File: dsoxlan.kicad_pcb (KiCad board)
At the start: 2 copper layers, 81.3 x 58.4 mm, 11 parts, among them P1 CNT-RJ45, P2 CONN_02X40

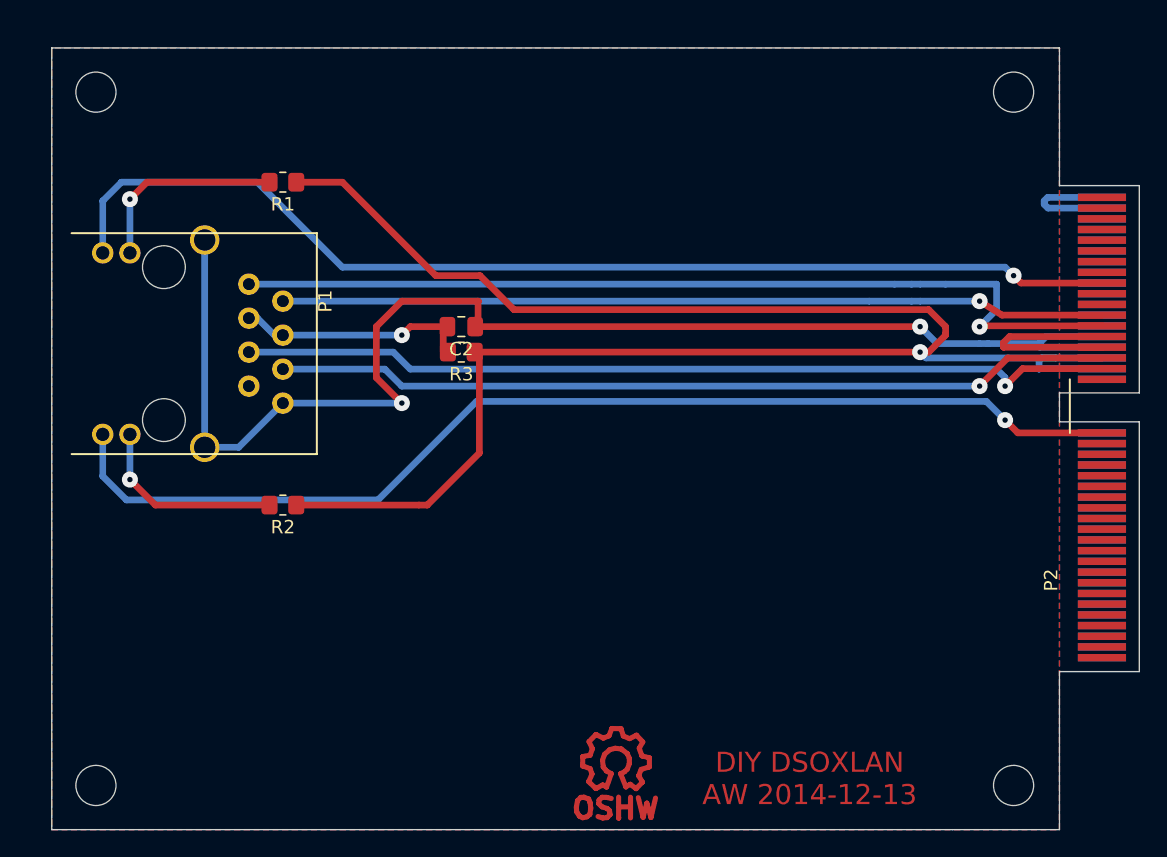
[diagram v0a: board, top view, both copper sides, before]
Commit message: DSC fixup
Replace all objects by new ones from the current libraries
shipped by Kicad.

This causes a slightly different OSHW (Opensource Hardware)
logo to be used in the PCB.

To maintain schematic parity, all mechanical objects on the
PCB (mounting holes and OSHW logo) have their schematic
counterparts now.
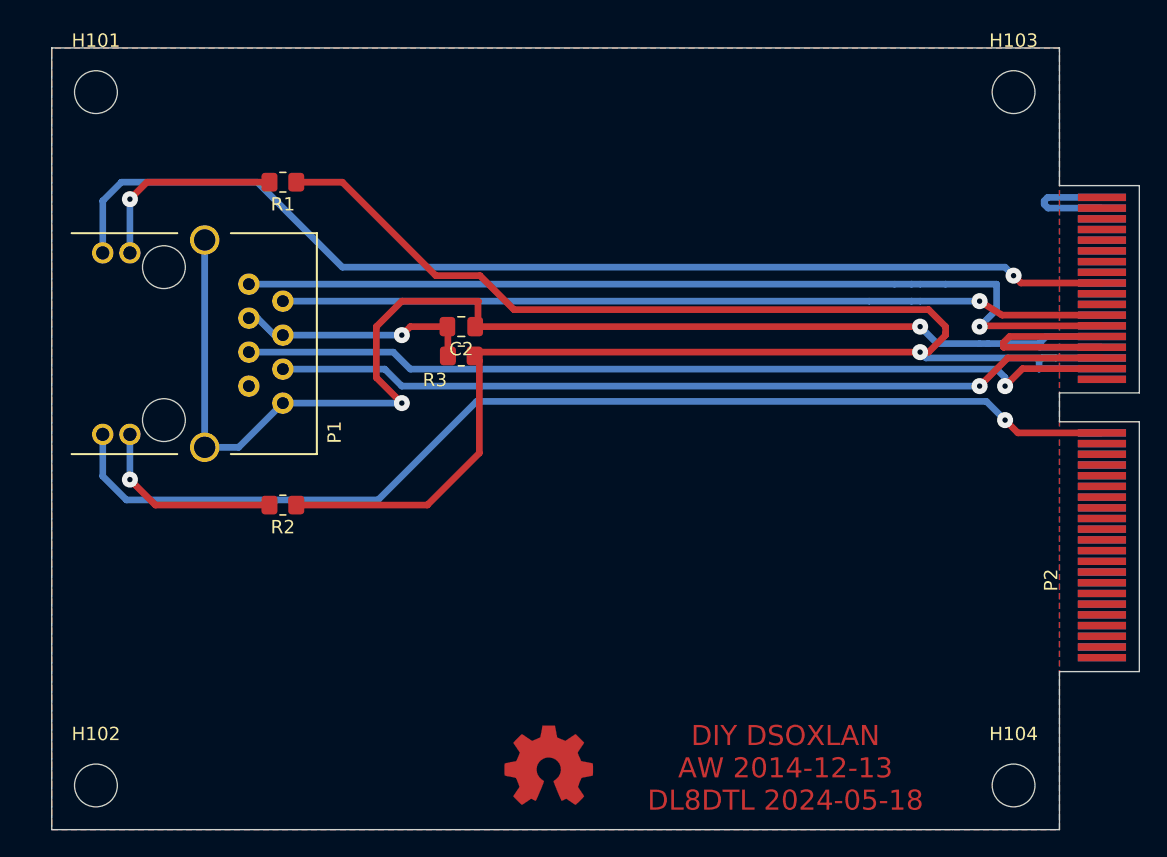
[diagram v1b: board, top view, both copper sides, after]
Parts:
- removed Symbol_OSHW-Logo_CopperTop: VAL**, Symbols:Symbol_OSHW-Logo_CopperTop
- added SYM101: Logo_Open_Hardware_Small, Symbol:OSHW-Symbol_6.7x6mm_Copper, F.Cu at (149.4, 112.8)
- H101, H102, H103, H104: renamed from MountingHole_3mm; value VAL** -> MountingHole; footprint Mounting_Holes:MountingHole_3mm -> MountingHole:MountingHole_3.2mm_M3_ISO7380
- moved R3 0.28 mm to (142.9, 82.2)
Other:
- board text added: "DIY DSOXLAN AW 2014-12-13 DL8DTL 2024-05-18"
- board text removed: "DIY DSOXLAN AW 2014-12-13"

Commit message: Replace RJ45 jack by Bel Fuse 08B0-1X1T-36-F
The old TE Connectivity device is no longer available.

Found another one that contains similar magnetics and
termination as the TE one.
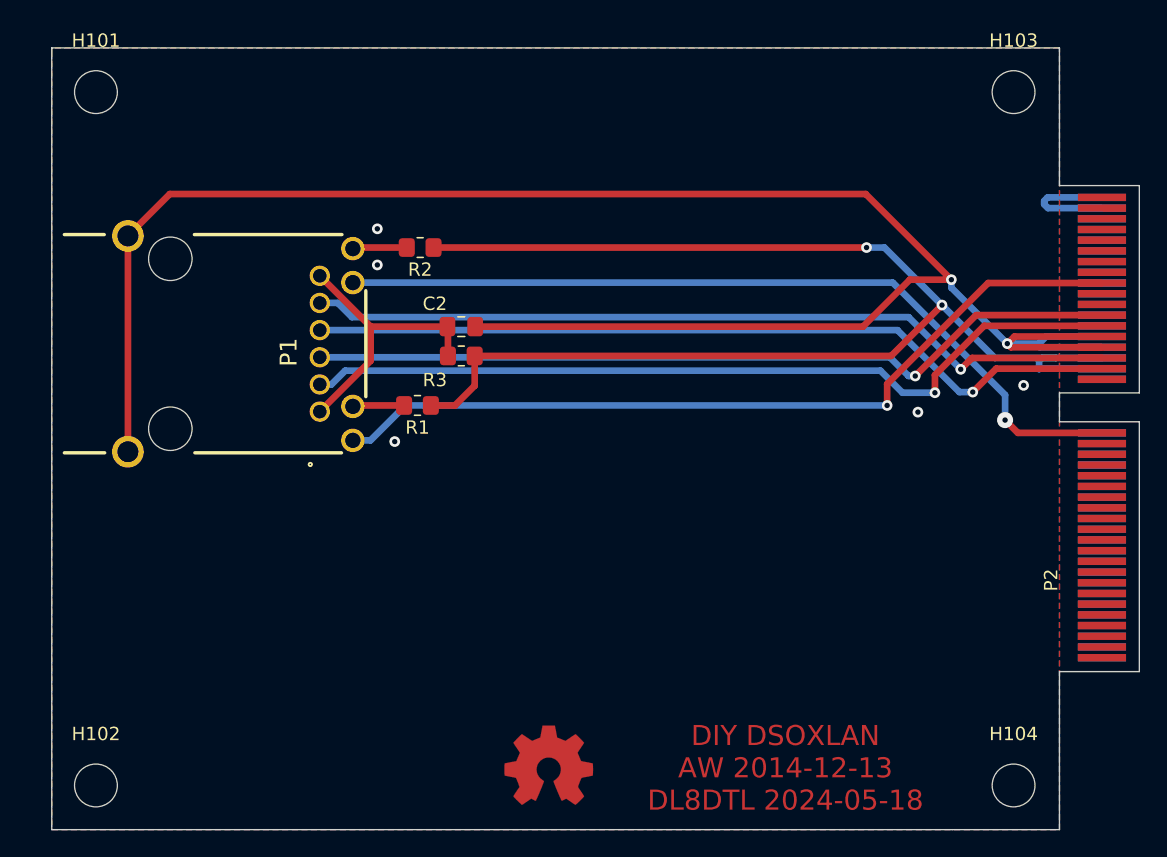
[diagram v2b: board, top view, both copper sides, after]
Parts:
- P1: value CNT-RJ45 -> 08B0-1X1T-36-F; footprint DSOXLAN:ETH-MAGJACK -> DSOXLAN:08B0-1X1T-36-F
- R1, R2: value 220R -> 470R
- moved R2 21.8 mm to (139.8, 74.1)
- moved R1 19.5 mm to (139.6, 85.9)
- moved P1 13.3 mm to (110.2, 89.4), turned to 90 degrees
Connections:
- P1 pad 1: RX+ -> Net-(C2-Pad2)
- P1 pad 10: GND -> Net-(P1-D4)
- P1 pad 13: Net-(P1-D3) -> GND
- P1 pad 14: LED2 -> GND
- P1 pad 2: RX- -> RX+
- P1 pad 3: Net-(C2-Pad2) -> RX-
- P1 pad 4: Net-(C2-Pad2) -> TX+
- P1 pad 5: TX+ -> TX-
- P1 pad 6: TX- -> Net-(C2-Pad2)
- P1 pad 7: unconnected-(P1-Pad7) -> LED1
- P1 pad 8: GND -> Net-(P1-D2)
- P1 pad 9: GND -> LED2
- R1 pad 2: Net-(P1-D1) -> Net-(P1-D2)
- R2 pad 2: Net-(P1-D3) -> Net-(P1-D4)
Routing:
- net GND: track 116.0 -> 151.9 mm, vias 2 -> 7
- net +3.3V: track 131.9 -> 102.7 mm, vias 1 -> 2
- net LED2: track 82.6 -> 61.7 mm
- net LED1: track 82.3 -> 61.8 mm
- net Net-(P1-D1): track 14.6 -> 0.00 mm, vias 1 -> 0
- net Net-(P1-D3): track 14.2 -> 0.00 mm, vias 1 -> 0
- net RX+: track 68.7 -> 62.4 mm
- net TX+: track 65.7 -> 61.1 mm
- net Net-(P1-D4): track 0.00 -> 4.06 mm
- net Net-(P1-D2): track 0.00 -> 3.86 mm
- net Net-(C2-Pad2): track 17.8 -> 21.2 mm, vias 1 -> 0
- net TX-: track 62.6 -> 60.9 mm
- net RX-: track 61.5 -> 60.9 mm

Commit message: Remove silkscreen prints for mounting holes
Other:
- board text added: "Bel Fuse 08B0-1X1T-36-F"
- board text removed: "ETH Magjack Digi-Key 1419-1021-ND"
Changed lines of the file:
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@@
     (property "ki_keywords" "mounting hole")
     (attr exclude_from_pos_files)
-    (fp_text reference "H102" (at 0 -3.85) (layer "F.SilkS")
+    (fp_text reference "H102" (at 0 -3.85) (layer "F.SilkS") hide
         (effects (font (size 1 1) (thickness 0.15)))
     )
@@
     (property "ki_keywords" "mounting hole")
     (attr exclude_from_pos_files)
-    (fp_text reference "H101" (at 0 -3.85) (layer "F.SilkS")
+    (fp_text reference "H101" (at 0 -3.85) (layer "F.SilkS") hide
         (effects (font (size 1 1) (thickness 0.15)))
     )
@@
     (property "ki_keywords" "mounting hole")
     (attr exclude_from_pos_files)
-    (fp_text reference "H103" (at 0 -3.85) (layer "F.SilkS")
+    (fp_text reference "H103" (at 0 -3.85) (layer "F.SilkS") hide
         (effects (font (size 1 1) (thickness 0.15)))
     )
@@
     (property "ki_keywords" "mounting hole")
     (attr exclude_from_pos_files)
-    (fp_text reference "H104" (at 0 -3.85) (layer "F.SilkS")
+    (fp_text reference "H104" (at 0 -3.85) (layer "F.SilkS") hide
         (effects (font (size 1 1) (thickness 0.15)))
     )
@@
     (effects (font (size 1.5 1.5) (thickness 0.3)))
   )
-  (gr_text "ETH Magjack\nDigi-Key 1419-1021-ND" (at 106.4 96.4 90) (layer "Cmts.User")
+  (gr_text "Bel Fuse\n08B0-1X1T-36-F" (at 106.4 96.4 90) (layer "Cmts.User")
     (effects (font (size 1.5 1.5) (thickness 0.3)) (justify left))
   )

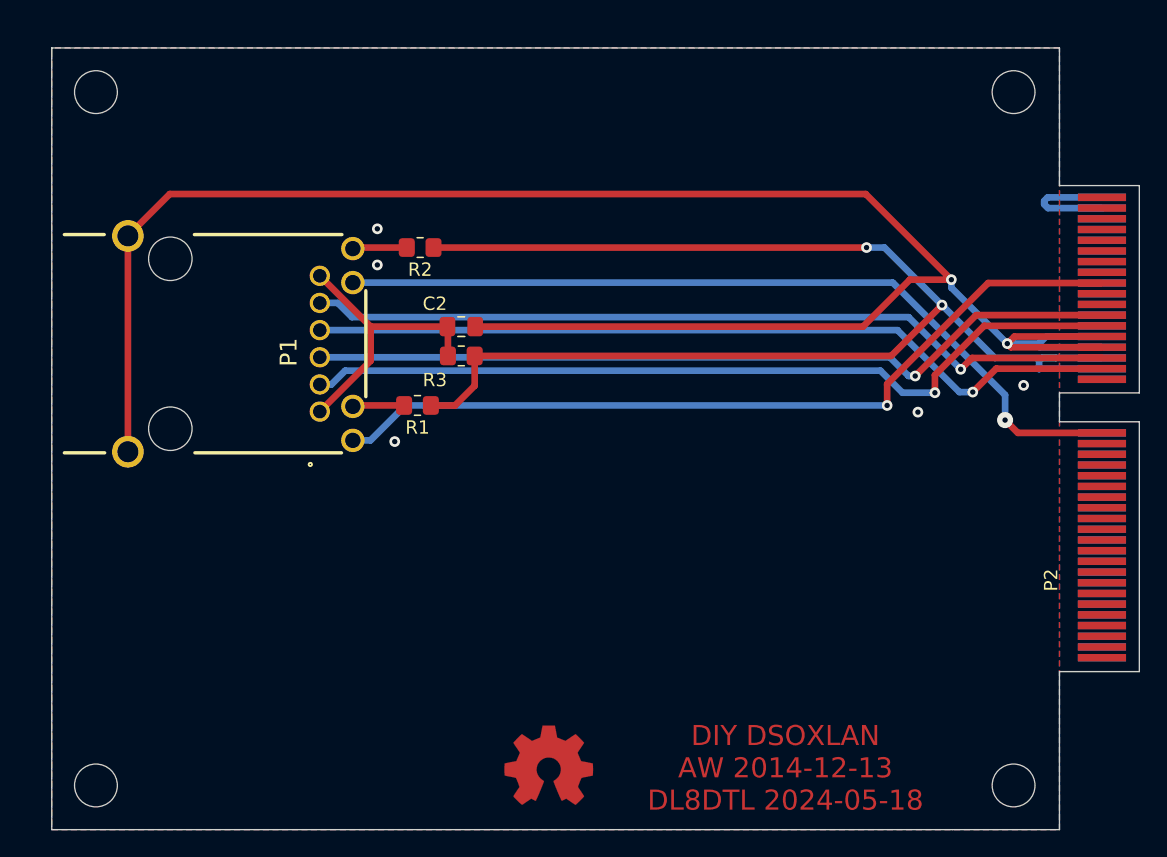
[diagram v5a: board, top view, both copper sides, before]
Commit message: Replace RJ45 jack by Würth 7499010121A
This one appears to be readily available at various distributors.

Also add 3D print models for case parts, obtained from

https://www.eevblog.com/forum/projects/diy-dsoxlan-interface-for-keysight-oscilloscopes/msg4323214/#msg4323214

apparently authored by Jay_Diddy_B.

Adapted layout to fit these models.
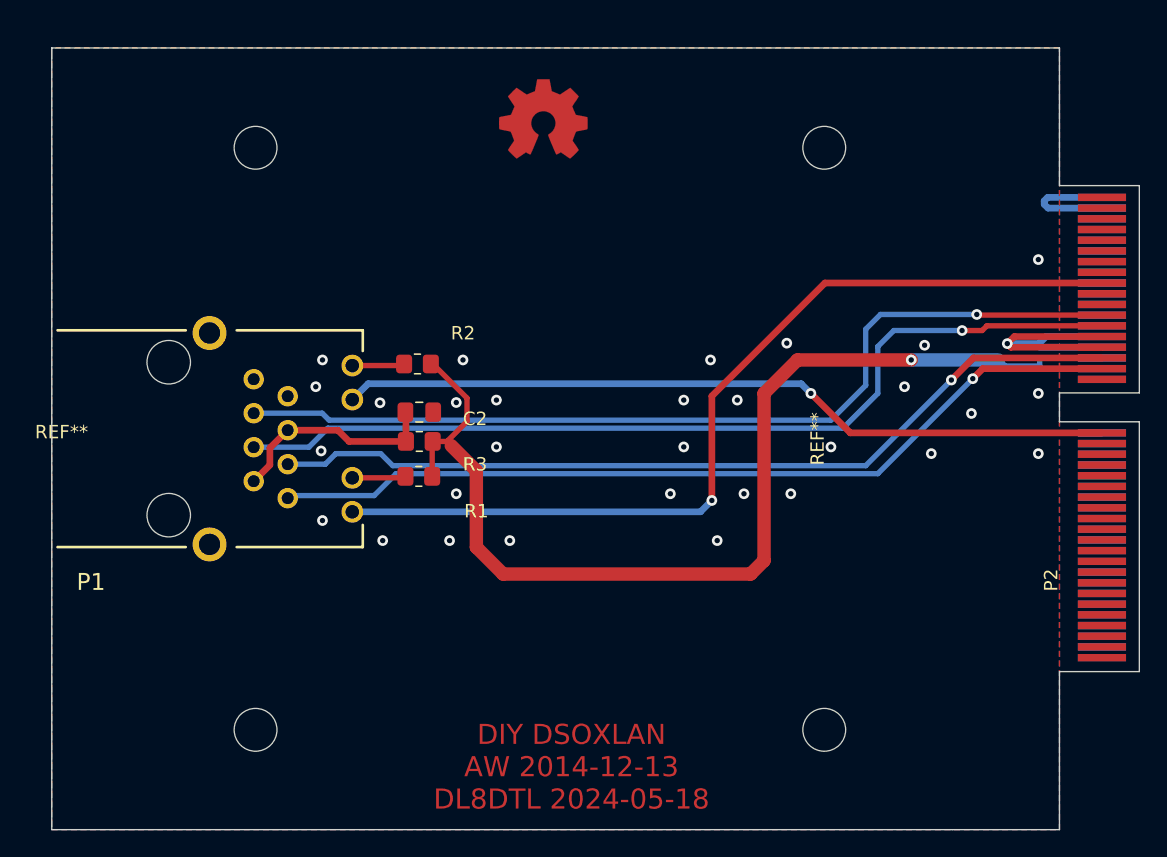
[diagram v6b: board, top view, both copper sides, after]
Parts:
- added REF**: Lid, DSOXLAN:Lid, F.Cu at (113.0, 88.4)
- added REF**: Spacer2b, DSOXLAN:Spacer2b, F.Cu at (170.0, 88.4)
- added REF**: Spacer1a, DSOXLAN:Spacer1a, B.Cu at (170.0, 88.4)
- P1: value 08B0-1X1T-36-F -> 7499010121A; footprint DSOXLAN:08B0-1X1T-36-F -> DSOXLAN:WURTH-7499010121A
- moved SYM101 48.3 mm to (149.0, 64.5)
- moved P1 20.0 mm to (129.9, 92.8)
- moved H104 14.7 mm to (170.0, 110.1)
- moved H103 14.7 mm to (170.0, 66.6)
- moved H101 12.6 mm to (127.5, 66.6)
- moved H102 12.6 mm to (127.5, 110.1)
- moved R2 8.70 mm to (139.6, 82.8)
- moved C2 7.12 mm to (139.7, 86.4)
- moved R3 7.12 mm to (139.7, 88.6)
- moved R1 5.30 mm to (139.7, 91.2)
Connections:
- C2 pad 2: Net-(C2-Pad2) -> Net-(P1-CRD)
- P1 pad 1: Net-(C2-Pad2) -> TX+
- P1 pad 10: Net-(P1-D4) -> Net-(P1-AG)
- P1 pad 2: RX+ -> Net-(P1-CRD)
- P1 pad 3: RX- -> TX-
- P1 pad 4: TX+ -> RX+
- P1 pad 5: TX- -> Net-(P1-CRD)
- P1 pad 6: Net-(C2-Pad2) -> RX-
- P1 pad 7: LED1 -> unconnected-(P1-NC-Pad7)
- P1 pad 8: Net-(P1-D2) -> GND
- P1 pad 9: LED2 -> LED1
- R1 pad 2: Net-(P1-D2) -> Net-(P1-AG)
- R2 pad 2: Net-(P1-D4) -> Net-(P1-AY)
- R3 pad 2: Net-(C2-Pad2) -> Net-(P1-CRD)
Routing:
- net GND: track 151.9 -> 26.7 mm, vias 7 -> 31
- net Net-(C2-Pad2): track 21.2 -> 0.00 mm
- net Net-(P1-CRD): track 0.00 -> 16.3 mm
- net +3.3V: track 102.7 -> 87.3 mm, vias 2 -> 1
- net RX-: track 60.9 -> 69.4 mm
- net RX+: track 62.4 -> 69.2 mm
- net LED1: track 61.8 -> 67.7 mm
- net Net-(P1-D4): track 4.06 -> 0.00 mm
- net TX-: track 60.9 -> 64.9 mm
- net Net-(P1-AG): track 0.00 -> 4.02 mm
- net Net-(P1-AY): track 0.00 -> 3.92 mm
- net Net-(P1-D2): track 3.86 -> 0.00 mm
- net TX+: track 61.1 -> 64.9 mm
- net LED2: track 61.7 -> 58.0 mm
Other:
- board text removed: "Bel Fuse 08B0-1X1T-36-F"
